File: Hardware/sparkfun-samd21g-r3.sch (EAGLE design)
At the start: 62 parts, among them Q1 2.5A/30V, Q2 2N7002PW, U1 MCP73831, U2 74AHC1G125, U3 MIC5219 3.3V, U4 ATSAMD21G-A, Y1 32.768kHz

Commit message: Pulling buffer up to VIN instead of 3.3V
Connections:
- net 3.3V: no longer R4.2, U2.VCC
- net VIN: now also R4.2, U2.VCC
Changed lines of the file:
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@@
 <setting verticaltext="up"/>
 </settings>
-<grid distance="0.1" unitdist="inch" unit="inch" style="lines" multiple="1" display="no" altdistance="0.01" altunitdist="inch" altunit="inch"/>
+<grid distance="0.1" unitdist="inch" unit="inch" style="lines" multiple="1" display="no" altdistance="0.005" altunitdist="inch" altunit="inch"/>
 <layers>
 <layer number="1" name="Top" color="4" fill="1" visible="no" active="no"/>
@@
 <part name="U2" library="SparkFun-DigitalIC" deviceset="74AHC1G125" device=""/>
 <part name="R4" library="SparkFun-Resistors" deviceset="100KOHM-1/10W-1%(0603)" device="" value="100k"/>
-<part name="SUPPLY2" library="SparkFun-Aesthetics" deviceset="3.3V" device=""/>
-<part name="SUPPLY4" library="SparkFun-Aesthetics" deviceset="3.3V" device=""/>
 <part name="GND9" library="SparkFun-Aesthetics" deviceset="GND" device=""/>
 <part name="R2" library="SparkFun-Resistors" deviceset="330OHM1/10W1%(0603)" device="" value="330"/>
@@
 <part name="R12" library="SparkFun-Resistors" deviceset="100KOHM-1/10W-1%(0603)" device="" value="100k"/>
 <part name="GND27" library="SparkFun-Aesthetics" deviceset="GND" device=""/>
+<part name="SUPPLY2" library="SparkFun-Aesthetics" deviceset="VIN" device=""/>
+<part name="SUPPLY4" library="SparkFun-Aesthetics" deviceset="VIN" device=""/>
 </parts>
 <sheets>
@@
 <instance part="U2" gate="G$1" x="86.36" y="25.4"/>
 <instance part="R4" gate="G$1" x="63.5" y="35.56" rot="R90"/>
-<instance part="SUPPLY2" gate="G$1" x="63.5" y="43.18"/>
-<instance part="SUPPLY4" gate="G$1" x="101.6" y="33.02"/>
 <instance part="GND9" gate="1" x="71.12" y="17.78"/>
 <instance part="R2" gate="G$1" x="55.88" y="27.94"/>
@@
 <instance part="R12" gate="G$1" x="208.28" y="213.36" rot="R90"/>
 <instance part="GND27" gate="1" x="208.28" y="203.2"/>
+<instance part="SUPPLY2" gate="G$1" x="63.5" y="43.18"/>
+<instance part="SUPPLY4" gate="G$1" x="101.6" y="43.18"/>
 </instances>
 <busses>
@@
 <wire x1="180.34" y1="165.1" x2="180.34" y2="167.64" width="0.1524" layer="91"/>
 <pinref part="SUPPLY8" gate="G$1" pin="3.3V"/>
-</segment>
-<segment>
-<pinref part="R4" gate="G$1" pin="2"/>
-<pinref part="SUPPLY2" gate="G$1" pin="3.3V"/>
-<wire x1="63.5" y1="43.18" x2="63.5" y2="40.64" width="0.1524" layer="91"/>
-</segment>
-<segment>
-<pinref part="U2" gate="G$1" pin="VCC"/>
-<pinref part="SUPPLY4" gate="G$1" pin="3.3V"/>
-<wire x1="99.06" y1="27.94" x2="101.6" y2="27.94" width="0.1524" layer="91"/>
-<wire x1="101.6" y1="27.94" x2="101.6" y2="33.02" width="0.1524" layer="91"/>
 </segment>
 <segment>
@@
 <wire x1="177.8" y1="93.98" x2="177.8" y2="96.52" width="0.1524" layer="91"/>
 </segment>
+<segment>
+<pinref part="R4" gate="G$1" pin="2"/>
+<pinref part="SUPPLY2" gate="G$1" pin="VIN"/>
+<wire x1="63.5" y1="43.18" x2="63.5" y2="40.64" width="0.1524" layer="91"/>
+</segment>
+<segment>
+<pinref part="U2" gate="G$1" pin="VCC"/>
+<wire x1="99.06" y1="27.94" x2="101.6" y2="27.94" width="0.1524" layer="91"/>
+<wire x1="101.6" y1="27.94" x2="101.6" y2="43.18" width="0.1524" layer="91"/>
+<pinref part="SUPPLY4" gate="G$1" pin="VIN"/>
+</segment>
 </net>
 <net name="A3" class="0">
@@
 <wire x1="63.5" y1="27.94" x2="60.96" y2="27.94" width="0.1524" layer="91"/>
 <pinref part="R2" gate="G$1" pin="2"/>
-</segment>
-</net>
+<wire x1="71.12" y1="25.4" x2="68.58" y2="25.4" width="0.1524" layer="91"/>
+<junction x="71.12" y="25.4"/>
+<label x="68.58" y="25.4" size="1.27" layer="95" rot="R180" xref="yes"/>
+</segment>
+</net>

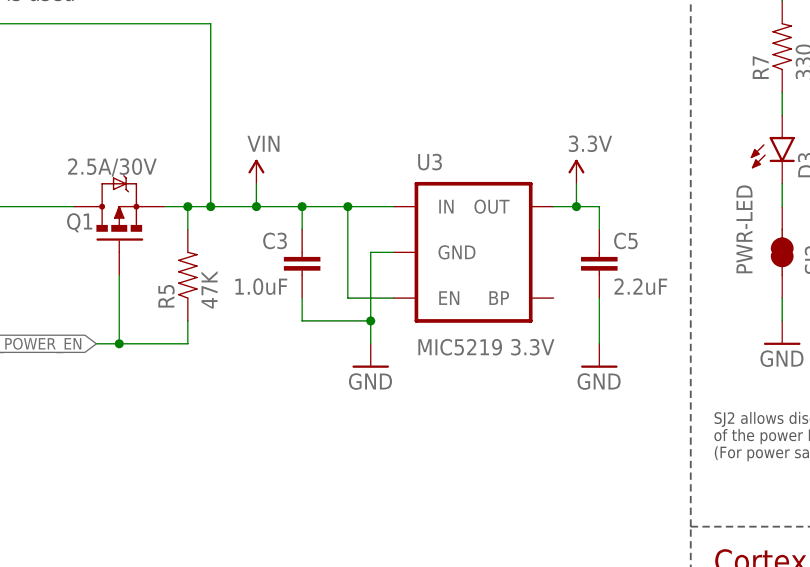
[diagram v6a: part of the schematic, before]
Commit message: Swapping MIC5205 Regulator out for AP2112K-3.3V
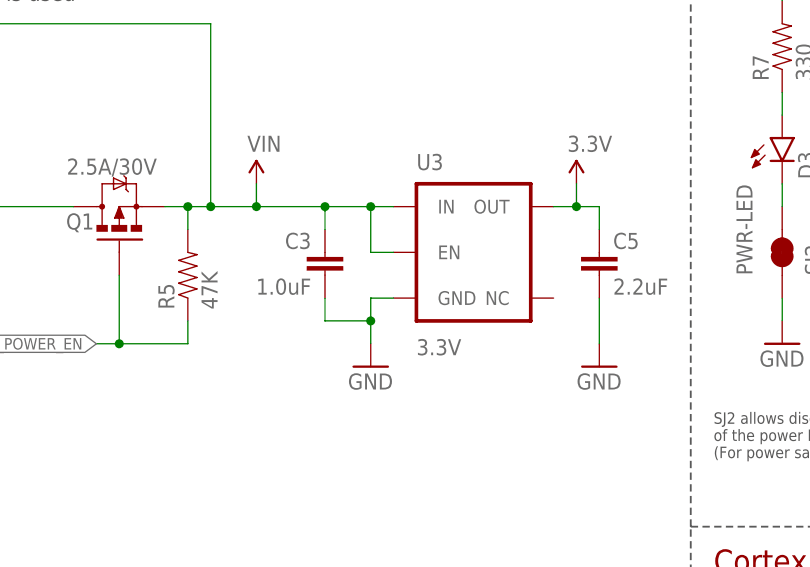
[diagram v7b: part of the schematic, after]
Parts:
- U3: value MIC5219 3.3V -> 3.3V; device SparkFun-PowerIC:V_REG_MIC52193.3V -> SparkFun-PowerIC:V_REG_AP2112K-3.3V
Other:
- moved on the sheet: C3
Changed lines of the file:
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@@
 <setting verticaltext="up"/>
 </settings>
-<grid distance="0.1" unitdist="inch" unit="inch" style="lines" multiple="1" display="no" altdistance="0.005" altunitdist="inch" altunit="inch"/>
+<grid distance="0.1" unitdist="inch" unit="inch" style="lines" multiple="1" display="no" altdistance="0.01" altunitdist="inch" altunit="inch"/>
 <layers>
 <layer number="1" name="Top" color="4" fill="1" visible="no" active="no"/>
@@
 <part name="GND1" library="SparkFun-Aesthetics" deviceset="GND" device=""/>
 <part name="GND22" library="SparkFun-Aesthetics" deviceset="GND" device=""/>
-<part name="U3" library="SparkFun-PowerIC" deviceset="V_REG_MIC5219" device="3.3V" value="MIC5219 3.3V"/>
+<part name="U3" library="SparkFun-PowerIC" deviceset="V_REG_AP2112" device="K-3.3V" value="3.3V"/>
 <part name="GND11" library="SparkFun-Aesthetics" deviceset="GND" device=""/>
 <part name="GND13" library="SparkFun-Aesthetics" deviceset="GND" device=""/>
@@
 <instance part="GND17" gate="1" x="198.12" y="203.2"/>
 <instance part="D4" gate="G$1" x="198.12" y="233.68"/>
-<instance part="C3" gate="G$1" x="99.06" y="218.44" rot="MR0"/>
+<instance part="C3" gate="G$1" x="101.6" y="218.44" rot="MR0"/>
 <instance part="C5" gate="G$1" x="132.08" y="218.44"/>
 <instance part="Q2" gate="G$1" x="198.12" y="220.98" rot="MR0"/>
@@
 <pinref part="U3" gate="G$1" pin="GND"/>
 <pinref part="GND11" gate="1" pin="GND"/>
-<wire x1="109.22" y1="220.98" x2="106.68" y2="220.98" width="0.1524" layer="91"/>
-<wire x1="106.68" y1="220.98" x2="106.68" y2="213.36" width="0.1524" layer="91"/>
+<wire x1="109.22" y1="215.9" x2="106.68" y2="215.9" width="0.1524" layer="91"/>
+<wire x1="106.68" y1="215.9" x2="106.68" y2="213.36" width="0.1524" layer="91"/>
 <wire x1="106.68" y1="213.36" x2="106.68" y2="210.82" width="0.1524" layer="91"/>
-<wire x1="99.06" y1="215.9" x2="99.06" y2="213.36" width="0.1524" layer="91"/>
-<wire x1="99.06" y1="213.36" x2="106.68" y2="213.36" width="0.1524" layer="91"/>
+<wire x1="101.6" y1="215.9" x2="101.6" y2="213.36" width="0.1524" layer="91"/>
+<wire x1="101.6" y1="213.36" x2="106.68" y2="213.36" width="0.1524" layer="91"/>
 <junction x="106.68" y="213.36"/>
 <pinref part="C3" gate="G$1" pin="2"/>
@@
 <net name="VIN" class="0">
 <segment>
-<wire x1="99.06" y1="223.52" x2="99.06" y2="226.06" width="0.1524" layer="91"/>
+<wire x1="101.6" y1="223.52" x2="101.6" y2="226.06" width="0.1524" layer="91"/>
 <pinref part="U3" gate="G$1" pin="IN"/>
-<wire x1="99.06" y1="226.06" x2="104.14" y2="226.06" width="0.1524" layer="91"/>
-<wire x1="104.14" y1="226.06" x2="109.22" y2="226.06" width="0.1524" layer="91"/>
-<junction x="99.06" y="226.06"/>
+<wire x1="101.6" y1="226.06" x2="106.68" y2="226.06" width="0.1524" layer="91"/>
+<wire x1="106.68" y1="226.06" x2="109.22" y2="226.06" width="0.1524" layer="91"/>
+<junction x="101.6" y="226.06"/>
 <pinref part="U3" gate="G$1" pin="EN"/>
-<wire x1="109.22" y1="215.9" x2="104.14" y2="215.9" width="0.1524" layer="91"/>
-<wire x1="104.14" y1="215.9" x2="104.14" y2="226.06" width="0.1524" layer="91"/>
-<junction x="104.14" y="226.06"/>
+<wire x1="109.22" y1="220.98" x2="106.68" y2="220.98" width="0.1524" layer="91"/>
+<wire x1="106.68" y1="220.98" x2="106.68" y2="226.06" width="0.1524" layer="91"/>
+<junction x="106.68" y="226.06"/>
 <wire x1="88.9" y1="226.06" x2="93.98" y2="226.06" width="0.1524" layer="91"/>
-<wire x1="93.98" y1="226.06" x2="99.06" y2="226.06" width="0.1524" layer="91"/>
+<wire x1="93.98" y1="226.06" x2="101.6" y2="226.06" width="0.1524" layer="91"/>
 <junction x="88.9" y="226.06"/>
 <pinref part="C3" gate="G$1" pin="1"/>

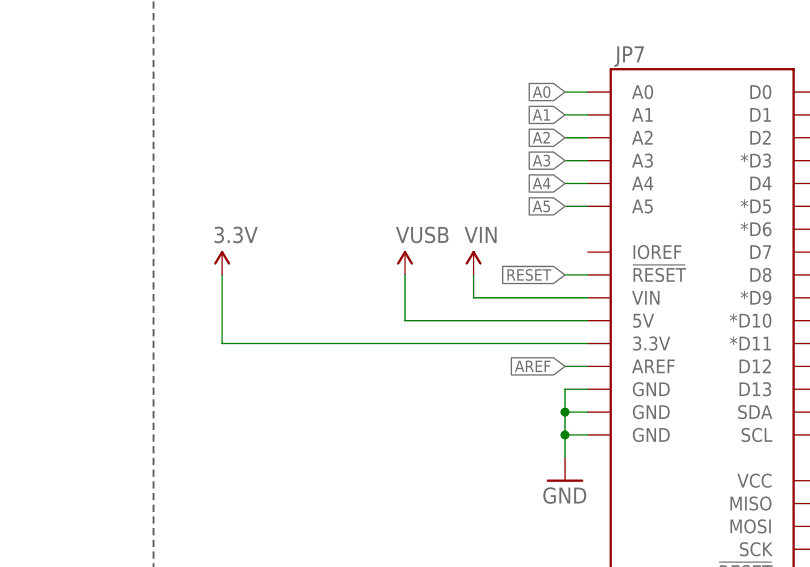
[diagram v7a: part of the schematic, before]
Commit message: Adding pin numbers to middle-board pins. Adding PWM indicators.
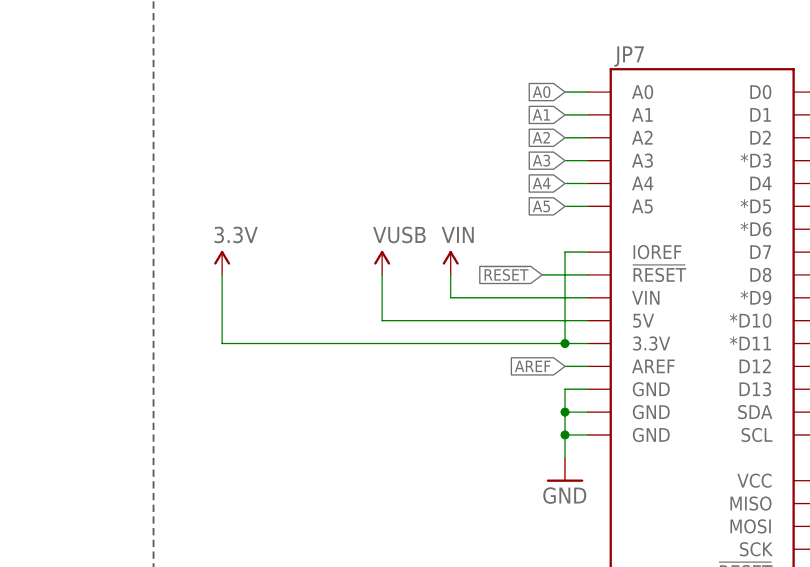
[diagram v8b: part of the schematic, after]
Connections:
- net 3.3V: now also JP7.IOREF
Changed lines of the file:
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@@
 <instance part="D1" gate="G$1" x="83.82" y="144.78"/>
 <instance part="SUPPLY16" gate="G$1" x="104.14" y="147.32"/>
-<instance part="SUPPLY17" gate="G$1" x="177.8" y="96.52"/>
+<instance part="SUPPLY17" gate="G$1" x="175.26" y="96.52"/>
 <instance part="SUPPLY18" gate="G$1" x="93.98" y="228.6"/>
-<instance part="SUPPLY3" gate="G$1" x="170.18" y="96.52"/>
+<instance part="SUPPLY3" gate="G$1" x="167.64" y="96.52"/>
 <instance part="SUPPLY5" gate="G$1" x="149.86" y="96.52"/>
 <instance part="SUPPLY19" gate="G$1" x="172.72" y="251.46"/>
@@
 <pinref part="JP7" gate="G$1" pin="3.3V"/>
 <pinref part="SUPPLY5" gate="G$1" pin="3.3V"/>
-<wire x1="190.5" y1="88.9" x2="149.86" y2="88.9" width="0.1524" layer="91"/>
+<wire x1="190.5" y1="88.9" x2="187.96" y2="88.9" width="0.1524" layer="91"/>
+<wire x1="187.96" y1="88.9" x2="149.86" y2="88.9" width="0.1524" layer="91"/>
 <wire x1="149.86" y1="88.9" x2="149.86" y2="96.52" width="0.1524" layer="91"/>
+<pinref part="JP7" gate="G$1" pin="IOREF"/>
+<wire x1="190.5" y1="99.06" x2="187.96" y2="99.06" width="0.1524" layer="91"/>
+<wire x1="187.96" y1="99.06" x2="187.96" y2="88.9" width="0.1524" layer="91"/>
+<junction x="187.96" y="88.9"/>
 </segment>
 <segment>
@@
 <segment>
 <pinref part="JP7" gate="G$1" pin="!RESET!@1"/>
-<wire x1="190.5" y1="96.52" x2="187.96" y2="96.52" width="0.1524" layer="91"/>
-<label x="187.96" y="96.52" size="1.27" layer="95" rot="R180" xref="yes"/>
+<wire x1="190.5" y1="96.52" x2="185.42" y2="96.52" width="0.1524" layer="91"/>
+<label x="185.42" y="96.52" size="1.27" layer="95" rot="R180" xref="yes"/>
 </segment>
 <segment>
@@
 <pinref part="JP7" gate="G$1" pin="VIN"/>
 <pinref part="SUPPLY17" gate="G$1" pin="VIN"/>
-<wire x1="190.5" y1="93.98" x2="177.8" y2="93.98" width="0.1524" layer="91"/>
-<wire x1="177.8" y1="93.98" x2="177.8" y2="96.52" width="0.1524" layer="91"/>
+<wire x1="190.5" y1="93.98" x2="175.26" y2="93.98" width="0.1524" layer="91"/>
+<wire x1="175.26" y1="93.98" x2="175.26" y2="96.52" width="0.1524" layer="91"/>
 </segment>
 <segment>
@@
 <pinref part="JP7" gate="G$1" pin="5V"/>
 <pinref part="SUPPLY3" gate="G$1" pin="VUSB"/>
-<wire x1="190.5" y1="91.44" x2="170.18" y2="91.44" width="0.1524" layer="91"/>
-<wire x1="170.18" y1="91.44" x2="170.18" y2="96.52" width="0.1524" layer="91"/>
-</segment>
-</net>
+<wire x1="190.5" y1="91.44" x2="167.64" y2="91.44" width="0.1524" layer="91"/>
+<wire x1="167.64" y1="91.44" x2="167.64" y2="96.52" width="0.1524" layer="91"/>
+</segment>
+</net>
